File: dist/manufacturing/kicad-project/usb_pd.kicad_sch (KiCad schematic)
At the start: 31 parts, among them J1 J1, Q1 Q1, Q2 CSD17484F4, Q3 CSD17484F4, U1 TPD4S480RUKR, U2 TPS26750SRSMR, U3 M24512-RMN6TP, U4 SN74LVC1G08DBVR

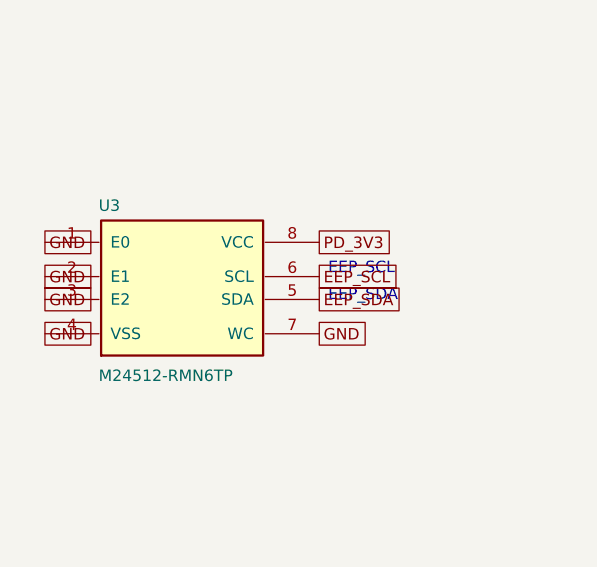
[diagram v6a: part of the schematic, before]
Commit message: Add routed diagnostics and isolated PD programming access
Add RGB and independent power indication, a reset-safe driven buzzer,
isolated EEPROM programming access, and eight power/programming probes.
Preserve top-side assembly and local bypass paths, and exclude all bare
service contacts from stencil paste.

Refresh firmware, Gerbers, BOM/CPL, 3D models and review documentation.
The full review passes 32 checks and 55 regression tests, with zero native
DRC, ERC, unconnected and schematic-parity issues. TI configuration and
physical qualification remain explicit order holds.
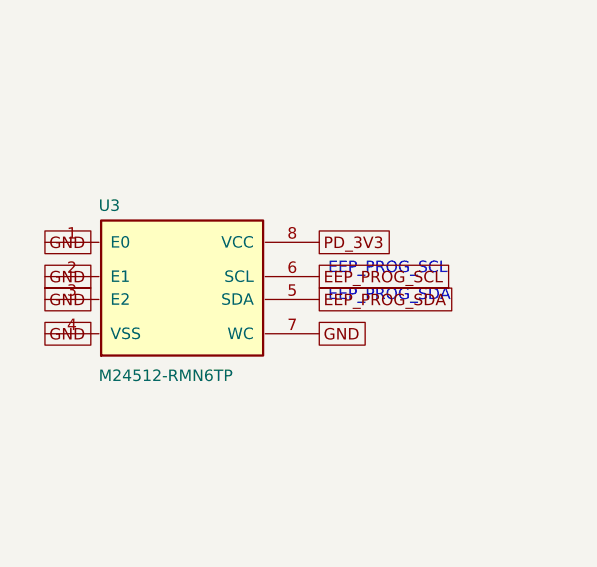
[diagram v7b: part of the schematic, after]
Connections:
- net EEP_SCL: no longer U3.6 (SCL)
- net EEP_SDA: no longer U3.5 (SDA)
- new net EEP_PROG_SCL: U3.6 (SCL)
- new net EEP_PROG_SDA: U3.5 (SDA)
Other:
- note added: "EEP_PROG_SCL"
- note added: "EEP_PROG_SDA"

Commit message: Fix source warnings and organize schematic on A4 sheets
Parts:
- removed C10, C9: 100nF, capacitor_cap0603, symbol Device:capacitor_down
- removed C3, C4: 220pF, capacitor_cap0603, symbol Device:capacitor_down
- removed C5: 4.7uF, capacitor_cap1206, symbol Device:capacitor_down
- removed C6, C7, C8: 10uF, capacitor_cap0603, symbol Device:capacitor_down
- removed Q2, Q3: CSD17484F4, CSD17484F4, symbol Device:U_CSD17484F4
- removed R11, R13, R15: 100kΩ, resistor_res0603, symbol Device:boxresistor_down
- removed R12, R9: 0Ω, resistor_res0603, symbol Device:boxresistor_right
- removed R14: 10kΩ, resistor_res0603, symbol Device:boxresistor_down
- removed R3, R4, R5, R6, R7: 4.7kΩ, resistor_res0603, symbol Device:boxresistor_down
- removed U2: TPS26750SRSMR, TPS26750SRSMR, symbol Device:U_TPS26750SRSMR
- removed U3: M24512-RMN6TP, M24512-RMN6TP, symbol Device:U_M24512-RMN6TP
- removed U4: SN74LVC1G08DBVR, SN74LVC1G08DBVR, symbol Device:U_SN74LVC1G08DBVR
- J1: value J1 -> USB4105-GF-A
- Q1: value Q1 -> BSS123LT1G
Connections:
- no-connect marks 10 -> 6
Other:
- note added: "J1: 48 V / 5 A EPR power only; USB DATA is on J10."
- note added: "U1 protects CC/VBUS. Q1 controls protected VBUS; C1/C2 provide local bypass."
- note removed: "EEP_IRQ_N"
- note removed: "EEP_PROG_SCL"
- note removed: "EEP_PROG_SDA"
- note removed: "EEP_SCL"
- note removed: "EEP_SDA"
- note removed: "EFUSE_EN"
- note removed: "J1 D+/D-: not connected. Q1: protected VBUS control. Q2/Q3: PD-path level translation."
- note removed: "J1: dedicated 48 V / 5 A EPR sink. USB DATA is on J10; the two VBUS rails are separate."
- note removed: "PD_INV_BASE"
- note removed: "PD_LEVEL_BASE"
- note removed: "PD_PATH_HV"
- note removed: "PD_PATH_N"
- note removed: "PD_PATH_OK"
- note removed: "PD_SCL"
- note removed: "PD_SDA"
- note removed: "POWER_PERMIT"
- note removed: "U1: 48 V CC/VBUS and unused SBU protection. U2: TPS26750 EPR sink controller. U3: PD policy EEPROM. U4: hardware power-permit gate."
